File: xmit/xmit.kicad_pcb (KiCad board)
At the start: 4 copper layers, 75 x 41 mm, 67 parts, among them J1 Conn_Coaxial, J2 Conn_01x02, J4 Conn_01x02, J5 Conn_01x02, J6 Conn_01x02, U1 74LVC1G66, U10 L7812, U11 SN74LVC1G04DBV, U12 74LVC1G66, U13 74LVC1G66, U2 74LVC1G66, U3 74LVC1G66, U4 74LVC1G66, U5 74LVC1G66, U6 74LVC1G66, U7 TPS7A20xxxDBV, U9 TLV760

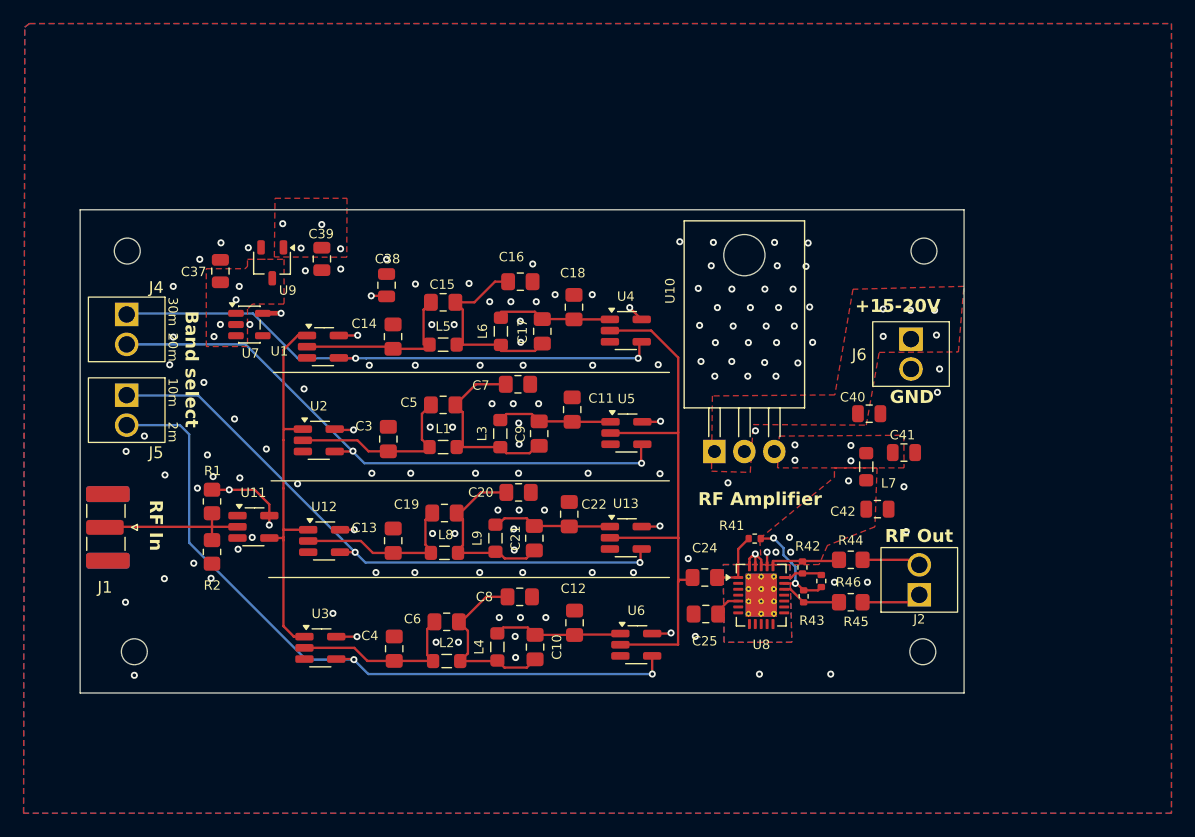
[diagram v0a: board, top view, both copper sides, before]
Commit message: More layout cleanup.
This is a checkpoint before I move all of the power management to a separate board. Next step is to move all power management to a separate board.
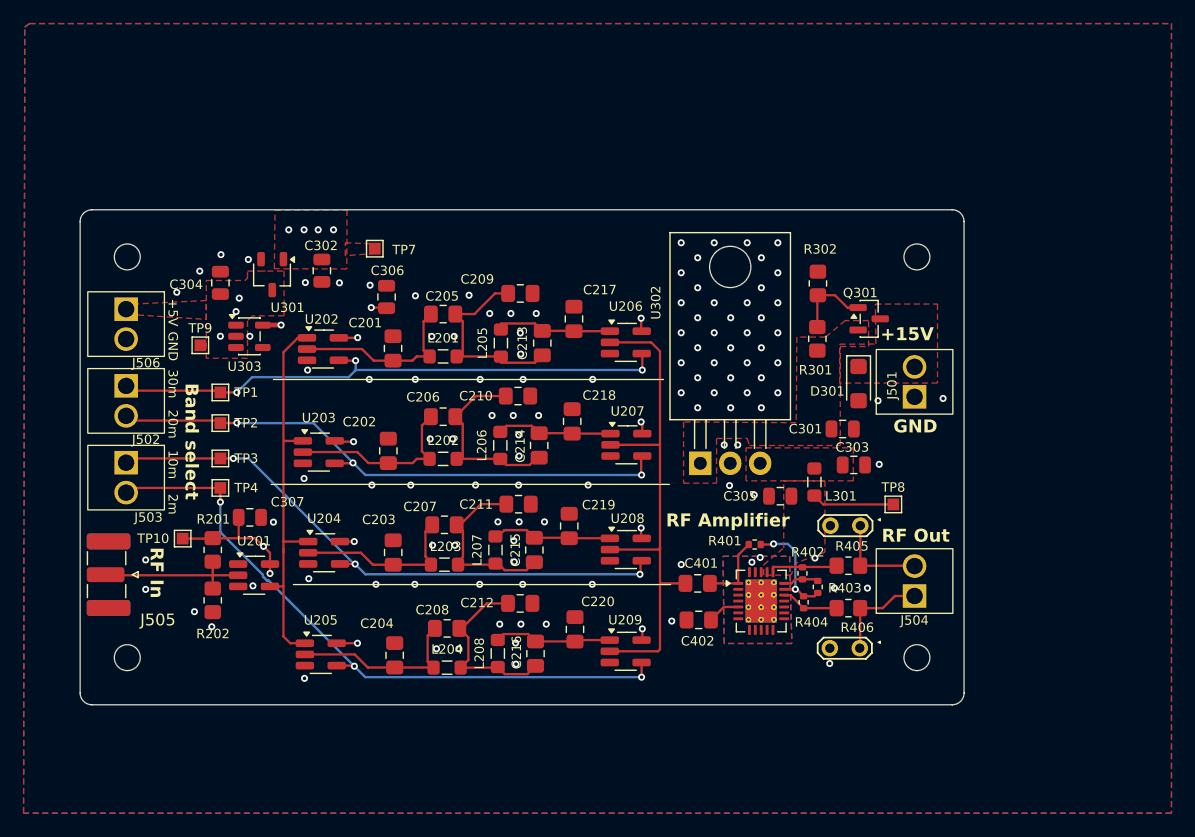
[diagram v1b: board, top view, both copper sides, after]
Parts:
- removed J6: Conn_01x02, Connector:terminal_block_02
- added C307: 1u, Capacitor_SMD:C_0805_2012Metric, F.Cu at (144.4, 77.1)
- added D301: SMF15A, Diode_SMD:D_SMF, F.Cu at (196.1, 65.8)
- added J501: Conn_01x02, Connector:terminal_block_02, F.Cu at (200.8, 65.6)
- added J506: Conn_01x02, Connector:terminal_block_02, F.Cu at (133.9, 60.7)
- added Q301: GSF3407, Package_TO_SOT_SMD:SOT-23, F.Cu at (196.9, 60.2)
- added R301: 100k, Resistor_SMD:R_0805_2012Metric_Pad1.20x1.40mm_HandSolder, F.Cu at (192.6, 62.0)
- added R302: 100k, Resistor_SMD:R_0805_2012Metric_Pad1.20x1.40mm_HandSolder, F.Cu at (192.6, 57.2)
- added TP1: 30m, TestPoint:TestPoint_Pad_1.0x1.0mm, F.Cu at (141.9, 66.5)
- added TP10: +3V3, TestPoint:TestPoint_Pad_1.0x1.0mm, F.Cu at (138.7, 78.9)
- added TP2: 20m, TestPoint:TestPoint_Pad_1.0x1.0mm, F.Cu at (141.9, 69.1)
- added TP3: 10m, TestPoint:TestPoint_Pad_1.0x1.0mm, F.Cu at (141.9, 72.1)
- added TP4: 2m, TestPoint:TestPoint_Pad_1.0x1.0mm, F.Cu at (141.9, 74.6)
- added TP5: out-, TestPoint:TestPoint_2Pads_Pitch2.54mm_Drill0.8mm, F.Cu at (196.2, 88.2)
- added TP6: out+, TestPoint:TestPoint_2Pads_Pitch2.54mm_Drill0.8mm, F.Cu at (196.2, 77.8)
- added TP7: +15V, TestPoint:TestPoint_Pad_1.0x1.0mm, F.Cu at (155.0, 54.3)
- added TP8: +12V, TestPoint:TestPoint_Pad_1.0x1.0mm, F.Cu at (199.0, 76.0)
- added TP9: +5V, TestPoint:TestPoint_Pad_1.0x1.0mm, F.Cu at (140.2, 62.5)
- moved C305 8.32 mm to (189.4, 75.3), turned to 0 degrees
- moved J502 6.07 mm to (133.9, 67.2)
- moved J503 5.73 mm to (133.9, 73.7)
- moved L301 4.59 mm to (192.3, 74.1)
- moved C303 4.38 mm to (195.7, 72.7)
- moved R201 4.11 mm to (141.3, 79.9)
- moved R202 4.11 mm to (141.3, 84.1)
- moved U201 4.11 mm to (144.8, 82.0)
- moved J505 4.01 mm to (132.2, 82.0)
- moved C301 2.60 mm to (194.7, 69.6)
- moved U302 1.56 mm to (182.6, 72.5)
- moved U209 1.06 mm to (176.3, 88.5)
- moved C201 1.00 mm to (156.6, 62.8)
- moved C202 1.00 mm to (156.2, 71.5)
- moved C203 1.00 mm to (156.6, 80.1)
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- renumbered C14 to C201, C3 to C202, C13 to C203, C4 to C204, C15 to C205, C5 to C206, C19 to C207, C6 to C208, C16 to C209, C7 to C210, C20 to C211, C8 to C212, C17 to C213, C9 to C214, C21 to C215, C10 to C216, C18 to C217, C11 to C218, C22 to C219, C12 to C220, C40 to C301, C39 to C302, C41 to C303, C37 to C304, C42 to C305, C38 to C306, C24 to C401, C25 to C402, H1 to H501, H2 to H502, H3 to H503, H4 to H504, J4 to J502, J5 to J503, J2 to J504, J1 to J505, L5 to L201, L1 to L202, L8 to L203, L2 to L204, L6 to L205, L3 to L206, L9 to L207, L4 to L208, L7 to L301, R1 to R201, R2 to R202, R41 to R401, R42 to R402, R46 to R403, R43 to R404, R44 to R405, R45 to R406, U11 to U201, U1 to U202, U2 to U203, U12 to U204, U3 to U205, U4 to U206, U5 to U207, U13 to U208, U6 to U209, U9 to U301, U10 to U302, U7 to U303, U8 to U401
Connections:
- net /Power/+20V renamed +15V
- net Net-(U1-Pad1) renamed drive
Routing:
- net Net-(Q301-G): track 0.00 -> 6.50 mm
- net band.2m: track 61.8 -> 55.8 mm, vias 2 -> 3
- net +12V: track 1.20 -> 7.01 mm, vias 5 -> 0
- net rf_drive: track 49.1 -> 45.2 mm
- net GND: track 3.46 -> 0.00 mm, vias 125 -> 117
- net out-: track 5.19 -> 8.63 mm
- net out+: track 4.88 -> 8.28 mm
- net +3V3: track 21.9 -> 24.8 mm
- net band.20m: track 51.2 -> 48.5 mm, vias 2 -> 3
- net band.10m: track 52.0 -> 50.6 mm, vias 2 -> 3
- net Net-(C216-Pad2): track 11.2 -> 9.86 mm
- net Net-(C201-Pad1): track 14.6 -> 15.5 mm
- net Net-(C202-Pad1): track 15.4 -> 16.0 mm
- net band.30m: track 48.1 -> 48.5 mm, vias 2 -> 3
- net /Power/raw12V: vias 4 -> 0
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- added copper zone on F.Cu, net +15V_raw
- removed copper zone on In2.Cu, net +12V
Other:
- board size 75 x 41 mm -> 75 x 42 mm
- board text added: "+15V"
- board text added: "+5V"
- board text removed: "+15-20V"

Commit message: changes up to first spin
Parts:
- removed the C301 at (194.7, 69.6)
- removed TP1: 30m, TestPoint:TestPoint_Pad_1.0x1.0mm
- removed TP10: +3V3, TestPoint:TestPoint_Pad_1.0x1.0mm
- removed TP2: 20m, TestPoint:TestPoint_Pad_1.0x1.0mm
- removed TP3: 10m, TestPoint:TestPoint_Pad_1.0x1.0mm
- removed TP4: 2m, TestPoint:TestPoint_Pad_1.0x1.0mm
- removed TP7: +15V, TestPoint:TestPoint_Pad_1.0x1.0mm
- removed TP8: +12V, TestPoint:TestPoint_Pad_1.0x1.0mm
- removed TP9: +5V, TestPoint:TestPoint_Pad_1.0x1.0mm
- removed the U301 at (146.3, 56.5)
- removed U302: L7812, Package_TO_SOT_THT:TO-220-3_Horizontal_TabDown
- added D201: LED, LED_SMD:LED_0603_1608Metric, F.Cu at (143.4, 65.9)
- added D202: LED, LED_SMD:LED_0603_1608Metric, F.Cu at (143.4, 68.5)
- added D203: LED, LED_SMD:LED_0603_1608Metric, F.Cu at (143.4, 72.4)
- added D204: LED, LED_SMD:LED_0603_1608Metric, F.Cu at (143.4, 74.9)
- added D302: LED, LED_SMD:LED_0603_1608Metric, F.Cu at (182.2, 56.2)
- added L302: 1µH, Inductor_SMD:L_0805_2012Metric_Pad1.05x1.20mm_HandSolder, F.Cu at (144.1, 54.8)
- added Q302: AO3407A, Package_TO_SOT_SMD:SOT-23, F.Cu at (140.7, 59.2)
- added R203: 100, Resistor_SMD:R_0603_1608Metric, F.Cu at (139.6, 66.0)
- added R204: 100, Resistor_SMD:R_0603_1608Metric, F.Cu at (139.6, 68.5)
- added R205: 100, Resistor_SMD:R_0603_1608Metric, F.Cu at (139.7, 72.4)
- added R206: 100, Resistor_SMD:R_0603_1608Metric, F.Cu at (139.7, 74.9)
- added R303: 200k, Resistor_SMD:R_0805_2012Metric_Pad1.20x1.40mm_HandSolder, F.Cu at (144.3, 59.1)
- added R304: 200k, Resistor_SMD:R_0805_2012Metric_Pad1.20x1.40mm_HandSolder, F.Cu at (142.8, 62.5)
- added R305: 2.2k, Resistor_SMD:R_0603_1608Metric, F.Cu at (185.2, 60.2)
- added R306: 100, Resistor_SMD:R_0603_1608Metric, F.Cu at (182.2, 60.2)
- C201, C217: value 220p -> 560p
- C202, C218: value 120p -> 270p
- C203, C219: value 50p -> 270p
- C205: value 12p -> 33p
- C206: value 8.1p -> 18p
- C207: value 3.9p -> 15p
- C209: value 330p -> 820p
- C210: value 200p -> 430p
- C211: value 81p -> 430p
- C212: value 72p -> 39p
- C213: value 31p -> 75pF
- C214: value 18p -> 39p
- C215: value 9p -> 33p
- C216: value 5.6p -> 10n
- C302: value 0.33µ -> 1µ
- C304: value 1u -> 1µ
- C305: renamed from C306; value 1u -> 1µ
- C306: renamed from C307; value 1u -> 1µ
- C401, C402: value 100n -> 10n
- D301: value SMF15A -> LED; footprint Diode_SMD:D_SMF -> LED_SMD:LED_0603_1608Metric
- H501, H502, H503, H504: value MountingHole -> ~
- J501: value Conn_01x02 -> ~; footprint Connector:terminal_block_02 -> TerminalBlock_TE-Connectivity:TerminalBlock_TE_282834-2_1x02_P2.54mm_Horizontal
- J502: renamed from J506; value Conn_01x02 -> ~; footprint Connector:terminal_block_02 -> TerminalBlock_TE-Connectivity:TerminalBlock_TE_282834-2_1x02_P2.54mm_Horizontal
- J503: renamed from J502; value Conn_01x02 -> ~; footprint Connector:terminal_block_02 -> TerminalBlock_TE-Connectivity:TerminalBlock_TE_282834-2_1x02_P2.54mm_Horizontal
- J504: renamed from J503; value Conn_01x02 -> ~; footprint Connector:terminal_block_02 -> TerminalBlock_TE-Connectivity:TerminalBlock_TE_282834-2_1x02_P2.54mm_Horizontal
- J505: renamed from J504; value Conn_01x02 -> ~; footprint Connector:terminal_block_02 -> TerminalBlock_TE-Connectivity:TerminalBlock_TE_282834-2_1x02_P2.54mm_Horizontal
- J506: renamed from J505; value Conn_Coaxial -> ~
- L201: value 2200n -> 810nH
- L202, L206: value 1600n -> 810nH
- L203, L207: value 800n -> 220nH
- L204, L208: value 56n -> 56nH
- L205: value 2000n -> 810nH
- L301: value 800µ -> 1µH
- Q301: value GSF3407 -> AO3407A
- R301, R302: value 100k -> 200k
- R403: value 237 -> 240
- R405, R406: value 2.5 -> 2
- TP501: renamed from TP5; value out- -> ~
- TP502: renamed from TP6; value out+ -> ~
- U201, U202, U203, U204, U205, U206, U207, U208, U209: footprint Package_TO_SOT_SMD:SOT-23-5_HandSoldering -> Package_TO_SOT_SMD:SOT-23-5
- U301: renamed from U303; value TPS7A20xxxDBV -> TPS7A2033PDBV
- U401: value ~ -> THS6222IRHFR
- moved D301 14.5 mm to (185.2, 56.2)
- moved C301 12.9 mm to (186.3, 63.8), turned to -90 degrees
- moved U301 10.2 mm to (151.6, 54.5)
- moved C302 8.64 mm to (141.9, 55.4), turned to -90 degrees
- moved L301 8.45 mm to (187.3, 67.2), turned to 0 degrees
- moved C303 8.44 mm to (191.4, 67.1), turned to 180 degrees
- moved C304 5.64 mm to (146.9, 54.6), turned to 90 degrees
- moved Q301 5.23 mm to (193.2, 64.0)
- moved C305 4.77 mm to (156.4, 53.6), turned to 180 degrees
- moved TP502 4.30 mm to (196.2, 73.5)
- moved R302 3.95 mm to (189.3, 59.5)
- moved R301 3.64 mm to (189.4, 63.9)
- moved R405 3.16 mm to (194.9, 78.0)
- moved C401 3.12 mm to (182.4, 79.6)
- moved R401 3.12 mm to (187.2, 76.3)
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- renumbered C303 to C301, C305 to C303
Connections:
- C301 pad 2: /Power/raw12V -> +15V_safe
- C302 pad 2: +15V -> +5V_safe
- C303 pad 2: +12V -> +15V
- D301 pad 1: +15V_raw -> GND
- D301 pad 2: GND -> Net-(D301-A)
- J502 pad 1: +5 -> +5V_raw
- L301 pad 1: /Power/raw12V -> +15V_safe
- L301 pad 2: +12V -> +15V
- Q301 pad 2: +15V -> +15V_safe
- R301 pad 2: +15V -> +15V_safe
- TP502 pad 2: GND -> (no net)
- U401 pad 21: +12V -> +15V
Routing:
- net +15V: track 0.00 -> 13.0 mm, vias 4 -> 0
- net +5V: track 0.00 -> 10.9 mm, vias 2 -> 0
- net +12V: track 7.01 -> 0.00 mm
- net +5V_safe: track 0.00 -> 6.81 mm
- net +5V_raw: track 0.00 -> 5.75 mm
- net Net-(Q302-G): track 0.00 -> 5.24 mm
- net Net-(D302-A): track 0.00 -> 2.44 mm
- net Net-(D301-A): track 0.00 -> 2.44 mm
- net Net-(D204-A): track 0.00 -> 2.44 mm
- net Net-(D203-A): track 0.00 -> 2.44 mm
- net Net-(D202-A): track 0.00 -> 2.44 mm
- net Net-(D201-A): track 0.00 -> 2.43 mm
- net band.20m: track 48.5 -> 50.1 mm
- net out+: track 8.28 -> 9.46 mm
- net band.30m: track 48.5 -> 49.7 mm
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- added copper zone on F.Cu, net +15V_safe
- added copper zone on F.Cu, net +3V3
- removed copper zone on F.Cu, net +12V
- removed copper zone on In2.Cu, net +15V
- removed copper zone on F.Cu, net +5V
- removed copper zone on In2.Cu, net +5V
- removed copper zone on F.Cu, net /Power/raw12V
- removed copper zone on In2.Cu, net /Power/raw12V
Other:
- outline, holes or cut-outs redrawn
- board text added: "15V"
- board text added: "3.3V"
- board text added: "Filters"
- board text added: "XMIT: Filter and RF amplifier"
- board text added: "https://github.com/tdunning/xmit"
- board text removed: "Band select"
